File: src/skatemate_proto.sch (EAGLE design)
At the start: 58 parts, among them IC1 REG1117, Q1 IRF740, Q2 IRF740, Q3 IRF740, Q4 IRF740, Q5 IRF740, Q6 IRF740, U1 DRV8301DCAR

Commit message: Further routing
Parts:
- added TP1, TP2, TP3, TP4, TP5: TPSMD_M_1006, skatemate:TPSMD_M_1006
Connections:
- net GND: now also TP2.TP
- net PH_A: now also TP3.TP
- net PH_B: now also TP4.TP
- net PH_C: now also TP5.TP
- net SUPPLY: now also TP1.TP
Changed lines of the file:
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@@
 <part name="P+6" library="supply1" deviceset="VCC" device=""/>
 <part name="P+7" library="supply1" deviceset="VCC" device=""/>
+<part name="TP1" library="skatemate" deviceset="TP" device="SMD_M_1006"/>
+<part name="TP2" library="skatemate" deviceset="TP" device="SMD_M_1006"/>
+<part name="TP3" library="skatemate" deviceset="TP" device="SMD_M_1006"/>
+<part name="TP4" library="skatemate" deviceset="TP" device="SMD_M_1006"/>
+<part name="TP5" library="skatemate" deviceset="TP" device="SMD_M_1006"/>
+<part name="GND12" library="supply1" deviceset="GND" device=""/>
 </parts>
 <sheets>
@@
 <instance part="FRAME2" gate="G$1" x="0" y="0"/>
 <instance part="FRAME2" gate="G$2" x="162.56" y="0"/>
+<instance part="TP1" gate="G$1" x="25.4" y="167.64" rot="R90"/>
+<instance part="TP2" gate="G$1" x="25.4" y="154.94" rot="R90"/>
+<instance part="TP3" gate="G$1" x="116.84" y="167.64" rot="R270"/>
+<instance part="TP4" gate="G$1" x="116.84" y="160.02" rot="R270"/>
+<instance part="TP5" gate="G$1" x="116.84" y="152.4" rot="R270"/>
+<instance part="GND12" gate="1" x="35.56" y="149.86"/>
 </instances>
 <busses>
@@
 <junction x="124.46" y="93.98"/>
 </segment>
+<segment>
+<pinref part="TP1" gate="G$1" pin="TP"/>
+<wire x1="27.94" y1="167.64" x2="35.56" y2="167.64" width="0.1524" layer="91"/>
+<label x="35.56" y="167.64" size="1.27" layer="95" xref="yes"/>
+</segment>
 </net>
 <net name="PH_B" class="0">
@@
 <label x="200.66" y="121.92" size="1.778" layer="95" rot="R90" xref="yes"/>
 </segment>
+<segment>
+<pinref part="TP4" gate="G$1" pin="TP"/>
+<wire x1="114.3" y1="160.02" x2="109.22" y2="160.02" width="0.1524" layer="91"/>
+<label x="109.22" y="160.02" size="1.27" layer="95" rot="R180" xref="yes"/>
+</segment>
 </net>
 <net name="PH_C" class="0">
@@
 <wire x1="233.68" y1="119.38" x2="233.68" y2="121.92" width="0.1524" layer="91"/>
 <label x="233.68" y="121.92" size="1.778" layer="95" rot="R90" xref="yes"/>
+</segment>
+<segment>
+<pinref part="TP5" gate="G$1" pin="TP"/>
+<wire x1="114.3" y1="152.4" x2="109.22" y2="152.4" width="0.1524" layer="91"/>
+<label x="109.22" y="152.4" size="1.27" layer="95" rot="R180" xref="yes"/>
 </segment>
 </net>
@@
 <wire x1="137.16" y1="93.98" x2="139.7" y2="93.98" width="0.1524" layer="91"/>
 </segment>
+<segment>
+<pinref part="TP2" gate="G$1" pin="TP"/>
+<wire x1="27.94" y1="154.94" x2="35.56" y2="154.94" width="0.1524" layer="91"/>
+<pinref part="GND12" gate="1" pin="GND"/>
+<wire x1="35.56" y1="152.4" x2="35.56" y2="154.94" width="0.1524" layer="91"/>
+</segment>
 </net>
 <net name="N$7" class="0">
@@
 <label x="167.64" y="121.92" size="1.778" layer="95" rot="R90" xref="yes"/>
 </segment>
-</net>
+<segment>
+<pinref part="TP3" gate="G$1" pin="TP"/>
+<wire x1="114.3" y1="167.64" x2="109.22" y2="167.64" width="0.1524" layer="91"/>
+<label x="109.22" y="167.64" size="1.27" layer="95" rot="R180" xref="yes"/>
+</segment>
+</net>

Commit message: Large junk of routing logic
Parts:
- added C25: (no value), skatemate:C-EUC0805
- added C26: 6n8, skatemate:C-EUC0805
- added C27: 120p, skatemate:C-EUC0805
- added D5: (no value), skatemate:SCHOTTKY-DIODESOD80C
- added R20, R21: (no value), skatemate:R-EU_R0805
- added R22: 15k, skatemate:R-EU_R0805
- added SV1, SV2: (no value), skatemate:MA12-1
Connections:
- new net N$20: C27.1, R22.2, U1.COMP
- new net N$21: C26.1, R22.1
- new net SSENSE: C25.1, D5.A, R20.1, R21.2, SV2.12
- net +5V: now also SV1.2
- net ASENSE: now also SV2.9
- net BSENSE: now also SV2.10
- net CSENSE: now also SV2.11
- net DRV_DCCAL: now also SV1.11
- net DRV_EN_GATE: now also SV1.12
- net DRV_NCS: now also SV1.7
- net DRV_NFAULT: now also SV1.6
- net DRV_NOCTW: now also SV1.5
- net DRV_PWRGD: now also SV1.4
- net DRV_SCK: now also SV1.10
- net DRV_SDI: now also SV1.8
- net DRV_SDO: now also SV1.9
- net DRV_SOA: now also SV2.7
- net DRV_SOB: now also SV2.8
- net GND: now also C25.2, C26.2, C27.2, R21.1, SV1.3
- net INH_A: now also SV2.1
- net INH_B: now also SV2.3
- net INH_C: now also SV2.5
- net INL_A: now also SV2.2
- net INL_B: now also SV2.4
- net INL_C: now also SV2.6
- net SUPPLY: now also R20.2
- net VCC: now also D5.C, SV1.1

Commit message: Added uC
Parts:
- added U2: STM32F303RCT6, skatemate:STM32F303RCT6
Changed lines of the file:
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@@
 <part name="C27" library="skatemate" deviceset="C-EU" device="C0805" value="120p"/>
 <part name="GND13" library="supply1" deviceset="GND" device=""/>
+<part name="FRAME3" library="frames" deviceset="DINA4_L" device=""/>
+<part name="U2" library="skatemate" deviceset="STM32F303RCT6" device=""/>
 </parts>
 <sheets>
@@
 </nets>
 </sheet>
+<sheet>
+<plain>
+</plain>
+<instances>
+<instance part="FRAME3" gate="G$1" x="0" y="0"/>
+<instance part="FRAME3" gate="G$2" x="162.56" y="0"/>
+<instance part="U2" gate="A" x="78.74" y="106.68"/>
+<instance part="U2" gate="B" x="198.12" y="106.68"/>
+</instances>
+<busses>
+</busses>
+<nets>
+</nets>
+</sheet>

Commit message: more digital layout
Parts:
- removed U2: STM32F303RCT6, skatemate:STM32F303RCT6
- added C28, C29, C33, C34: 2u2, skatemate:C-EUC0805
- added C30, C31, C32, C35, C36: 100n, skatemate:C-EUC0805
- added J1: (no value), skatemate:47346-0001
- added R23: 100k, skatemate:R-EU_R0805
- added R24, R25: 22, skatemate:R-EU_R0805
- added R26: 1k5, skatemate:R-EU_R0805
- added R27: 0 *, skatemate:R-EU_R0805
- added SV3: (no value), skatemate:MA06-1
- added U$3: STM32F303XD/XE, skatemate:STM32F303XD/XE
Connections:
- new net N$22: J1.4, R23.1
- new net N$23: J1.3, R24.1, R26.1
- new net N$24: J1.2, R25.1
- new net N$25: J1.1, R27.1
- new net NRST: SV3.5, U$3G$1.NRST
- new net SWCLK: SV3.2, U$3G$2.PA14
- new net SWDIO: SV3.4, U$3G$2.PA13
- new net USB_D+: R24.2, U$3G$2.PA12
- new net USB_D-: R25.2, U$3G$2.PA11
- net ASENSE: now also U$3G$1.PA2
- net BSENSE: now also U$3G$1.PA1
- net CSENSE: now also U$3G$1.PA0
- net DRV_DCCAL: now also U$3G$2.PC7
- net DRV_EN_GATE: now also U$3G$2.PC6
- net DRV_NCS: now also U$3G$2.PA15
- net DRV_NFAULT: now also U$3G$2.PD2
- net DRV_NOCTW: now also U$3G$2.PB3
- net DRV_PWRGD: now also U$3G$2.PB4
- net DRV_SCK: now also U$3G$2.PC10
- net DRV_SDI: now also U$3G$2.PC12
- net DRV_SDO: now also U$3G$2.PC11
- net DRV_SOA: now also U$3G$1.PB1
- net DRV_SOB: now also U$3G$1.PB0
- net GND: now also C28.1, C29.1, C30.1, C31.1, C32.1, C33.1, C34.1, C35.1, C36.1, J1.5, R23.2, SV3.3, U$3G$1.VSSA/VREF-, U$3G$1.VSS_2, U$3G$1.VSS_4, U$3G$2.VSS_1, U$3G$2.VSS_3
- net INH_A: now also U$3G$2.PA10
- net INH_B: now also U$3G$2.PA9
- net INH_C: now also U$3G$2.PA8
- net INL_A: now also U$3G$2.PB15
- net INL_B: now also U$3G$2.PB14
- net INL_C: now also U$3G$2.PB13
- net SSENSE: now also U$3G$1.PC3
- net VCC: now also C28.2, C29.2, C30.2, C31.2, C32.2, C33.2, C34.2, C35.2, C36.2, R26.2, R27.2, SV3.1, U$3G$1.VBAT, U$3G$1.VDDA, U$3G$1.VDD_2, U$3G$1.VDD_4, U$3G$2.VDD_1, U$3G$2.VDD_3

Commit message: lqfp64 and layout
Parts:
- U$3: value STM32F303XD/XE -> STM32F303XD/XELQFP64; device skatemate:STM32F303XD/XE -> skatemate:STM32F303XD/XELQFP64
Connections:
- net +5V: now also SV1.3; no longer SV1.2
- net GND: now also SV1.2; no longer SV1.3
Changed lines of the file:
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@@
 <part name="C36" library="skatemate" deviceset="C-EU" device="C0805" value="100n"/>
 <part name="GND19" library="supply1" deviceset="GND" device=""/>
-<part name="U$3" library="skatemate" deviceset="STM32F303XD/XE" device=""/>
+<part name="U$3" library="skatemate" deviceset="STM32F303XD/XE" device="LQFP64"/>
 </parts>
 <sheets>
@@
 </segment>
 <segment>
-<pinref part="SV1" gate="1" pin="3"/>
-<wire x1="172.72" y1="66.04" x2="177.8" y2="66.04" width="0.1524" layer="91"/>
-<label x="177.8" y="66.04" size="1.016" layer="95" xref="yes"/>
+<pinref part="SV1" gate="1" pin="2"/>
+<wire x1="172.72" y1="68.58" x2="177.8" y2="68.58" width="0.1524" layer="91"/>
+<label x="177.8" y="68.58" size="1.016" layer="95" xref="yes"/>
 </segment>
 </net>
@@
 </segment>
 <segment>
-<pinref part="SV1" gate="1" pin="2"/>
-<wire x1="172.72" y1="68.58" x2="177.8" y2="68.58" width="0.1524" layer="91"/>
-<label x="177.8" y="68.58" size="1.016" layer="95" xref="yes"/>
+<pinref part="SV1" gate="1" pin="3"/>
+<wire x1="172.72" y1="66.04" x2="177.8" y2="66.04" width="0.1524" layer="91"/>
+<label x="177.8" y="66.04" size="1.016" layer="95" xref="yes"/>
 </segment>
 </net>
@@
 <wire x1="55.88" y1="66.04" x2="50.8" y2="66.04" width="0.1524" layer="91"/>
 <junction x="50.8" y="66.04"/>
-<pinref part="U$3" gate="G$1" pin="VSSA/VREF-"/>
-<pinref part="U$3" gate="G$1" pin="VSS_2"/>
-<pinref part="U$3" gate="G$1" pin="VSS_4"/>
 <wire x1="55.88" y1="71.12" x2="50.8" y2="71.12" width="0.1524" layer="91"/>
 <wire x1="50.8" y1="71.12" x2="50.8" y2="68.58" width="0.1524" layer="91"/>
 <junction x="50.8" y="68.58"/>
-</segment>
-<segment>
+<pinref part="U$3" gate="G$1" pin="VSS_4"/>
+<pinref part="U$3" gate="G$1" pin="VSSA/VREF-"/>
+<pinref part="U$3" gate="G$1" pin="VSS_2"/>
+</segment>
+<segment>

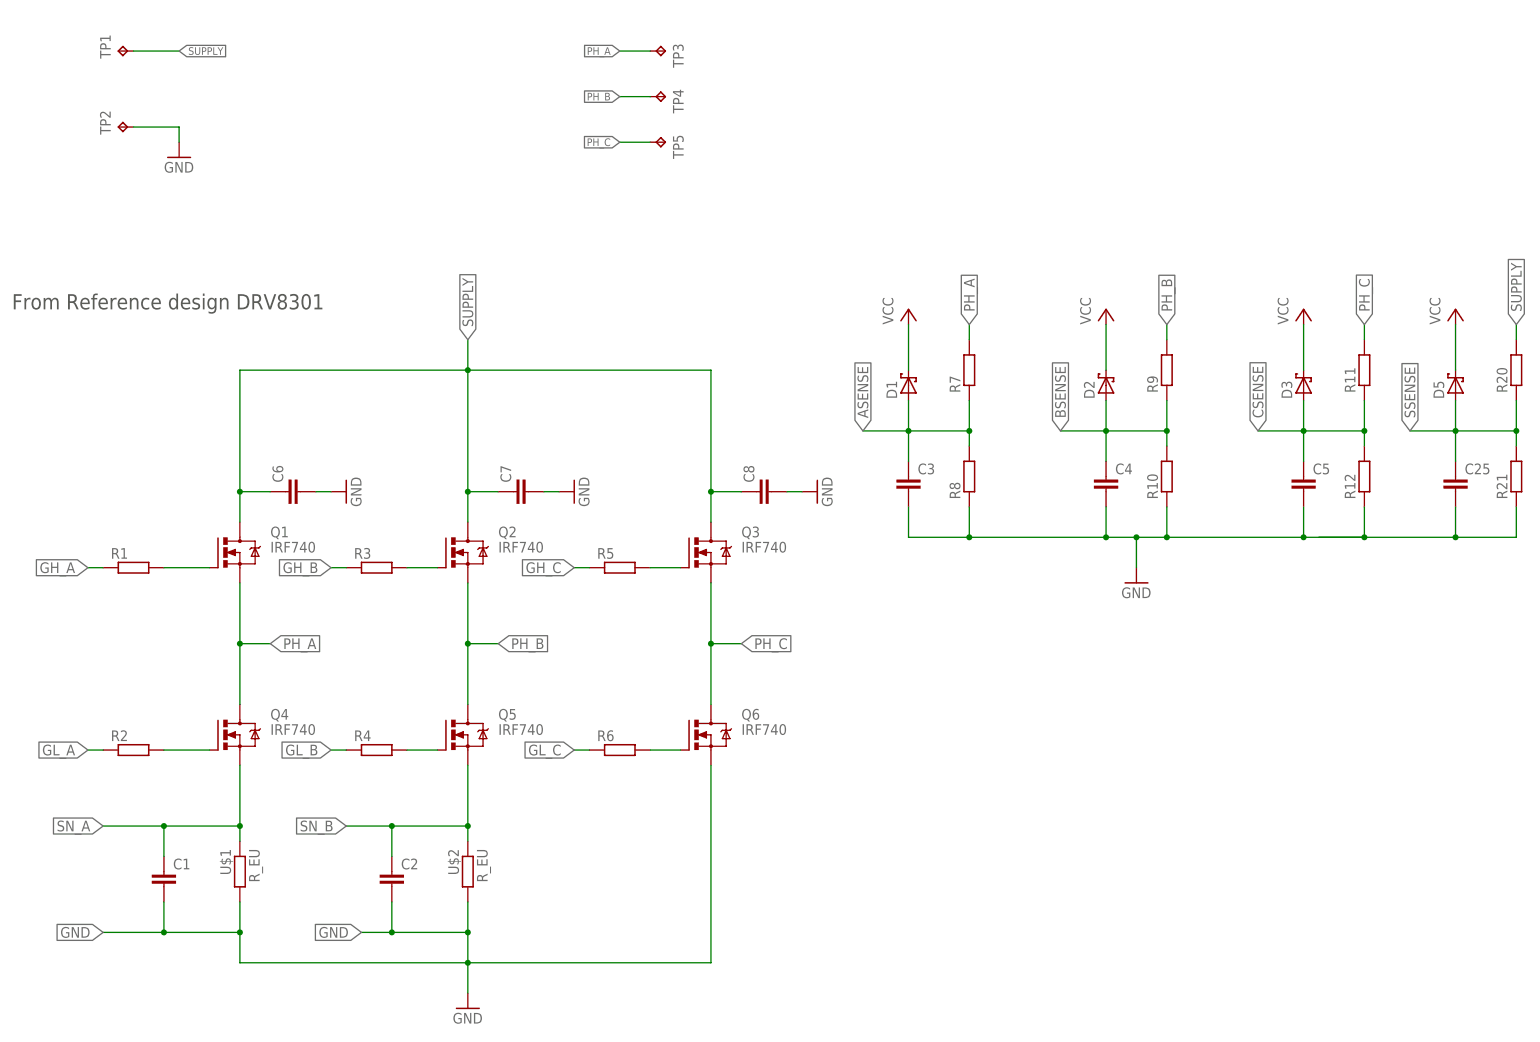
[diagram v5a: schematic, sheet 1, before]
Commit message: IRFS7534 added
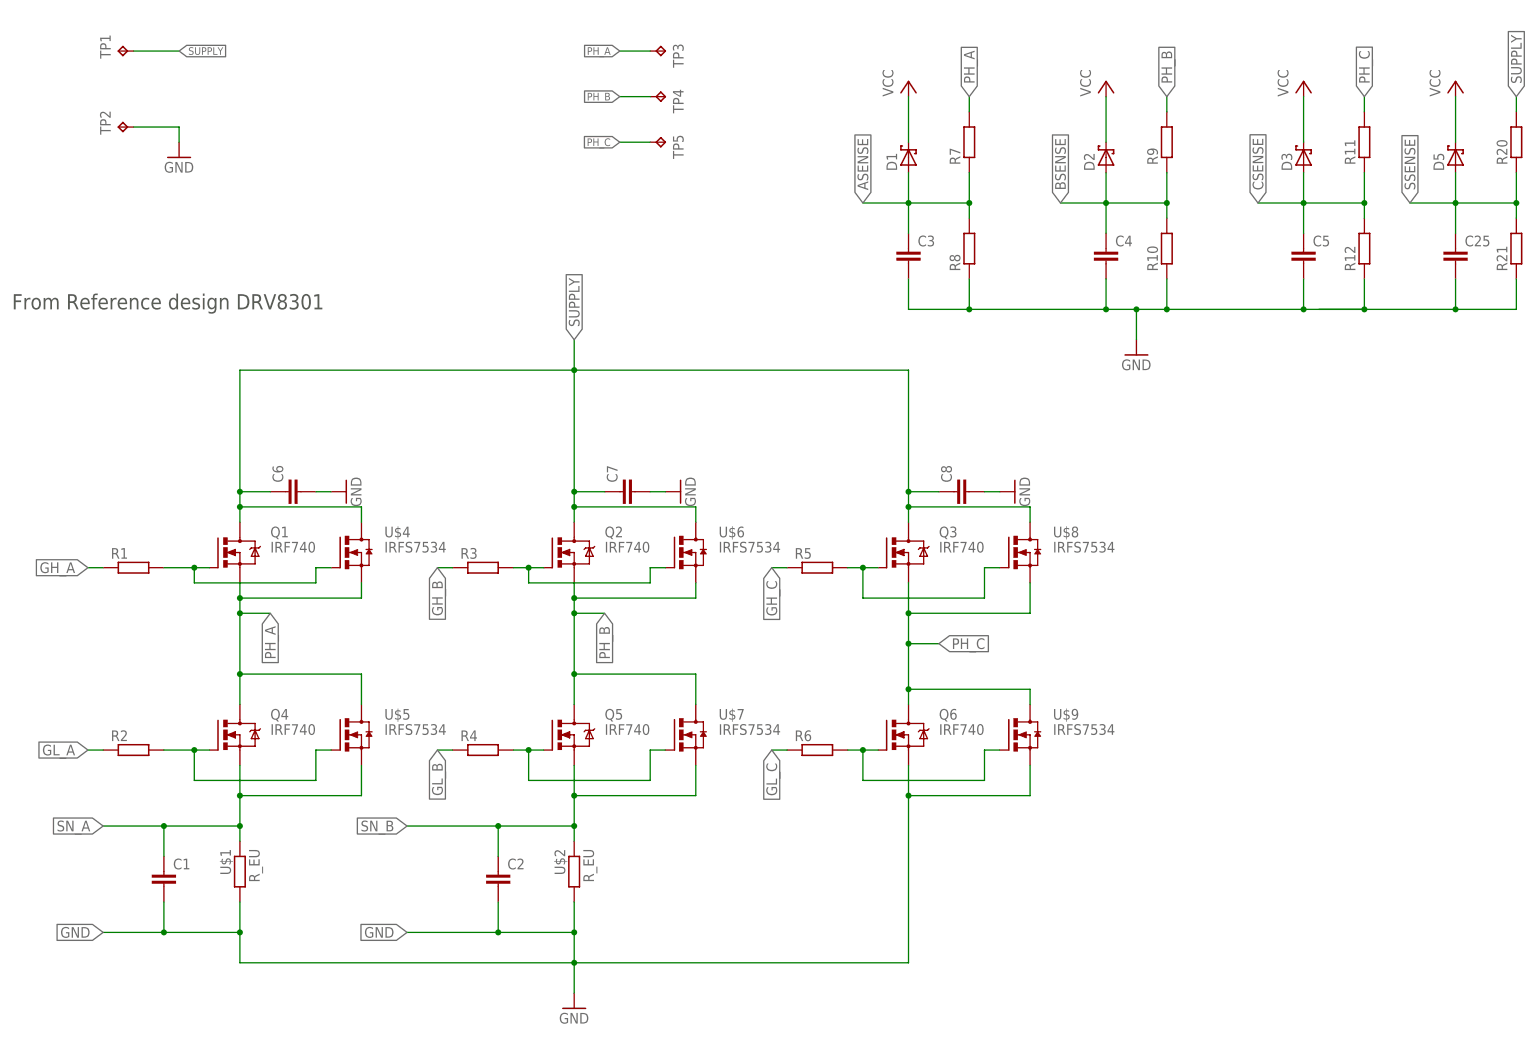
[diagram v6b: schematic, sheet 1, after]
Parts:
- added U$4, U$5, U$6, U$7, U$8, U$9: IRFS7534, skatemate:IRFS7534
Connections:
- net GND: now also U$9.S
- net N$10: now also U$6.G
- net N$11: now also U$8.G
- net N$12: now also U$9.G
- net N$7: now also U$4.G
- net N$8: now also U$5.G
- net N$9: now also U$7.G
- net PH_A: now also U$4.S, U$5.D
- net PH_B: now also U$6.S, U$7.D
- net PH_C: now also U$8.S, U$9.D
- net SN_A: now also U$5.S
- net SN_B: now also U$7.S
- net SUPPLY: now also U$4.D, U$6.D, U$8.D
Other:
- moved on the sheet: C2, C25, C3, C4, C5, C7, C8, D1, D2, D3, D5, Q2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
